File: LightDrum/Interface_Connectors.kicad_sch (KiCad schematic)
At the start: 6 parts, among them J6 0525593652, J7 0541323662, J8 PWR-CONN

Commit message: General component placement
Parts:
- J1203: renamed from J8; footprint Connector_JST:JST_XA_B02B-XASK-1_1x02_P2.50mm_Vertical -> Daxxn_Connectors:JST_XH_B2B-XH-A_Vertical
- renumbered C88 to C1201, C89 to C1202, C90 to C1203, J6 to J1201, J7 to J1202
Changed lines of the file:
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@@
   (symbol (lib_id "Device:C_Small") (at 31.75 22.86 0) (unit 1)
     (in_bom yes) (on_board yes)
-    (property "Reference" "C90" (id 0) (at 32.004 21.082 0)
+    (property "Reference" "C1203" (id 0) (at 32.004 21.082 0)
       (effects (font (size 1.27 1.27)) (justify left))
     )
@@
   (symbol (lib_id "power:GND") (at 50.8 93.98 0) (unit 1)
     (in_bom yes) (on_board yes)
-    (property "Reference" "#PWR0134" (id 0) (at 50.8 100.33 0)
+    (property "Reference" "#PWR01212" (id 0) (at 50.8 100.33 0)
       (effects (font (size 1.27 1.27)) hide)
     )
@@
   (symbol (lib_id "power:VCC") (at 25.4 20.32 0) (unit 1)
     (in_bom yes) (on_board yes)
-    (property "Reference" "#PWR0128" (id 0) (at 25.4 24.13 0)
+    (property "Reference" "#PWR01202" (id 0) (at 25.4 24.13 0)
       (effects (font (size 1.27 1.27)) hide)
     )
@@
   (symbol (lib_id "Daxxn_Connectors:0541323662") (at 123.19 86.36 0) (unit 1)
     (in_bom no) (on_board no)
-    (property "Reference" "J7" (id 0) (at 124.46 38.1 0))
+    (property "Reference" "J1202" (id 0) (at 124.46 38.1 0))
     (property "Value" "0541323662" (id 1) (at 124.46 40.64 0))
     (property "Footprint" "Daxxn_Connectors:0541323662" (id 2) (at 123.19 86.36 0)
@@
   (symbol (lib_id "power:VCC") (at 19.05 20.32 0) (unit 1)
     (in_bom yes) (on_board yes)
-    (property "Reference" "#PWR0127" (id 0) (at 19.05 24.13 0)
+    (property "Reference" "#PWR01201" (id 0) (at 19.05 24.13 0)
       (effects (font (size 1.27 1.27)) hide)
     )
@@
   (symbol (lib_id "power:GND") (at 25.4 25.4 0) (unit 1)
     (in_bom yes) (on_board yes)
-    (property "Reference" "#PWR0129" (id 0) (at 25.4 31.75 0)
+    (property "Reference" "#PWR01205" (id 0) (at 25.4 31.75 0)
       (effects (font (size 1.27 1.27)) hide)
     )
@@
   (symbol (lib_id "power:GND") (at 124.46 137.16 0) (unit 1)
     (in_bom yes) (on_board yes)
-    (property "Reference" "#PWR0133" (id 0) (at 124.46 143.51 0)
+    (property "Reference" "#PWR01216" (id 0) (at 124.46 143.51 0)
       (effects (font (size 1.27 1.27)) hide)
     )
@@
   (symbol (lib_id "Device:C_Small") (at 25.4 22.86 0) (unit 1)
     (in_bom yes) (on_board yes)
-    (property "Reference" "C89" (id 0) (at 25.654 21.082 0)
+    (property "Reference" "C1202" (id 0) (at 25.654 21.082 0)
       (effects (font (size 1.27 1.27)) (justify left))
     )
@@
   (symbol (lib_id "Device:C_Small") (at 19.05 22.86 0) (unit 1)
     (in_bom yes) (on_board yes)
-    (property "Reference" "C88" (id 0) (at 19.304 21.082 0)
+    (property "Reference" "C1201" (id 0) (at 19.304 21.082 0)
       (effects (font (size 1.27 1.27)) (justify left))
     )
@@
   (symbol (lib_id "power:VCC") (at 69.85 44.45 0) (unit 1)
     (in_bom yes) (on_board yes)
-    (property "Reference" "#PWR0123" (id 0) (at 69.85 48.26 0)
+    (property "Reference" "#PWR01210" (id 0) (at 69.85 48.26 0)
       (effects (font (size 1.27 1.27)) hide)
     )
@@
   (symbol (lib_id "power:GND") (at 50.8 114.3 0) (unit 1)
     (in_bom yes) (on_board yes)
-    (property "Reference" "#PWR0135" (id 0) (at 50.8 120.65 0)
+    (property "Reference" "#PWR01214" (id 0) (at 50.8 120.65 0)
       (effects (font (size 1.27 1.27)) hide)
     )
@@
   (symbol (lib_id "power:VCC") (at 91.44 40.64 0) (unit 1)
     (in_bom yes) (on_board yes)
-    (property "Reference" "#PWR0125" (id 0) (at 91.44 44.45 0)
+    (property "Reference" "#PWR01207" (id 0) (at 91.44 44.45 0)
       (effects (font (size 1.27 1.27)) hide)
     )
@@
   (symbol (lib_id "power:VCC") (at 31.75 20.32 0) (unit 1)
     (in_bom yes) (on_board yes)
-    (property "Reference" "#PWR0130" (id 0) (at 31.75 24.13 0)
+    (property "Reference" "#PWR01203" (id 0) (at 31.75 24.13 0)
       (effects (font (size 1.27 1.27)) hide)
     )
@@
   (symbol (lib_id "power:GND") (at 31.75 25.4 0) (unit 1)
     (in_bom yes) (on_board yes)
-    (property "Reference" "#PWR0131" (id 0) (at 31.75 31.75 0)
+    (property "Reference" "#PWR01206" (id 0) (at 31.75 31.75 0)
       (effects (font (size 1.27 1.27)) hide)
     )
@@
   (symbol (lib_id "power:Vdrive") (at 99.06 40.64 0) (unit 1)
     (in_bom yes) (on_board yes)
-    (property "Reference" "#PWR0132" (id 0) (at 93.98 44.45 0)
+    (property "Reference" "#PWR01208" (id 0) (at 93.98 44.45 0)
       (effects (font (size 1.27 1.27)) hide)
     )
@@
   (symbol (lib_id "power:VDD") (at 97.79 128.27 0) (unit 1)
     (in_bom yes) (on_board yes)
-    (property "Reference" "#PWR069" (id 0) (at 97.79 132.08 0)
+    (property "Reference" "#PWR01215" (id 0) (at 97.79 132.08 0)
       (effects (font (size 1.27 1.27)) hide)
     )
@@
   (symbol (lib_id "power:Vdrive") (at 63.5 44.45 0) (unit 1)
     (in_bom yes) (on_board yes)
-    (property "Reference" "#PWR0124" (id 0) (at 58.42 48.26 0)
+    (property "Reference" "#PWR01209" (id 0) (at 58.42 48.26 0)
       (effects (font (size 1.27 1.27)) hide)
     )
@@
   (symbol (lib_id "Connector:Conn_01x02_Male") (at 57.15 110.49 0) (mirror y) (unit 1)
     (in_bom yes) (on_board yes)
-    (property "Reference" "J8" (id 0) (at 58.42 110.49 0)
+    (property "Reference" "J1203" (id 0) (at 58.42 110.49 0)
       (effects (font (size 1.27 1.27)) (justify right))
     )
@@
       (effects (font (size 1.27 1.27)) (justify right))
     )
-    (property "Footprint" "Connector_JST:JST_XA_B02B-XASK-1_1x02_P2.50mm_Vertical" (id 2) (at 57.15 110.49 0)
+    (property "Footprint" "Daxxn_Connectors:JST_XH_B2B-XH-A_Vertical" (id 2) (at 57.15 110.49 0)
       (effects (font (size 1.27 1.27)) hide)
     )
@@
   (symbol (lib_id "power:VDD") (at 29.21 88.9 0) (unit 1)
     (in_bom yes) (on_board yes)
-    (property "Reference" "#PWR068" (id 0) (at 29.21 92.71 0)
+    (property "Reference" "#PWR01211" (id 0) (at 29.21 92.71 0)
       (effects (font (size 1.27 1.27)) hide)
     )
@@
   (symbol (lib_id "power:GND") (at 19.05 25.4 0) (unit 1)
     (in_bom yes) (on_board yes)
-    (property "Reference" "#PWR0126" (id 0) (at 19.05 31.75 0)
+    (property "Reference" "#PWR01204" (id 0) (at 19.05 31.75 0)
       (effects (font (size 1.27 1.27)) hide)
     )
@@
   (symbol (lib_id "power:VCC") (at 50.8 109.22 0) (unit 1)
     (in_bom yes) (on_board yes)
-    (property "Reference" "#PWR0136" (id 0) (at 50.8 113.03 0)
+    (property "Reference" "#PWR01213" (id 0) (at 50.8 113.03 0)
       (effects (font (size 1.27 1.27)) hide)
     )
@@
   (symbol (lib_id "Daxxn_Connectors:0525593652") (at 52.07 71.12 180) (unit 1)
     (in_bom yes) (on_board yes)
-    (property "Reference" "J6" (id 0) (at 50.8 40.64 0))
+    (property "Reference" "J1201" (id 0) (at 50.8 40.64 0))
     (property "Value" "0525593652" (id 1) (at 50.8 43.18 0))
     (property "Footprint" "Daxxn_Connectors:0525593652" (id 2) (at 50.8 99.06 0)

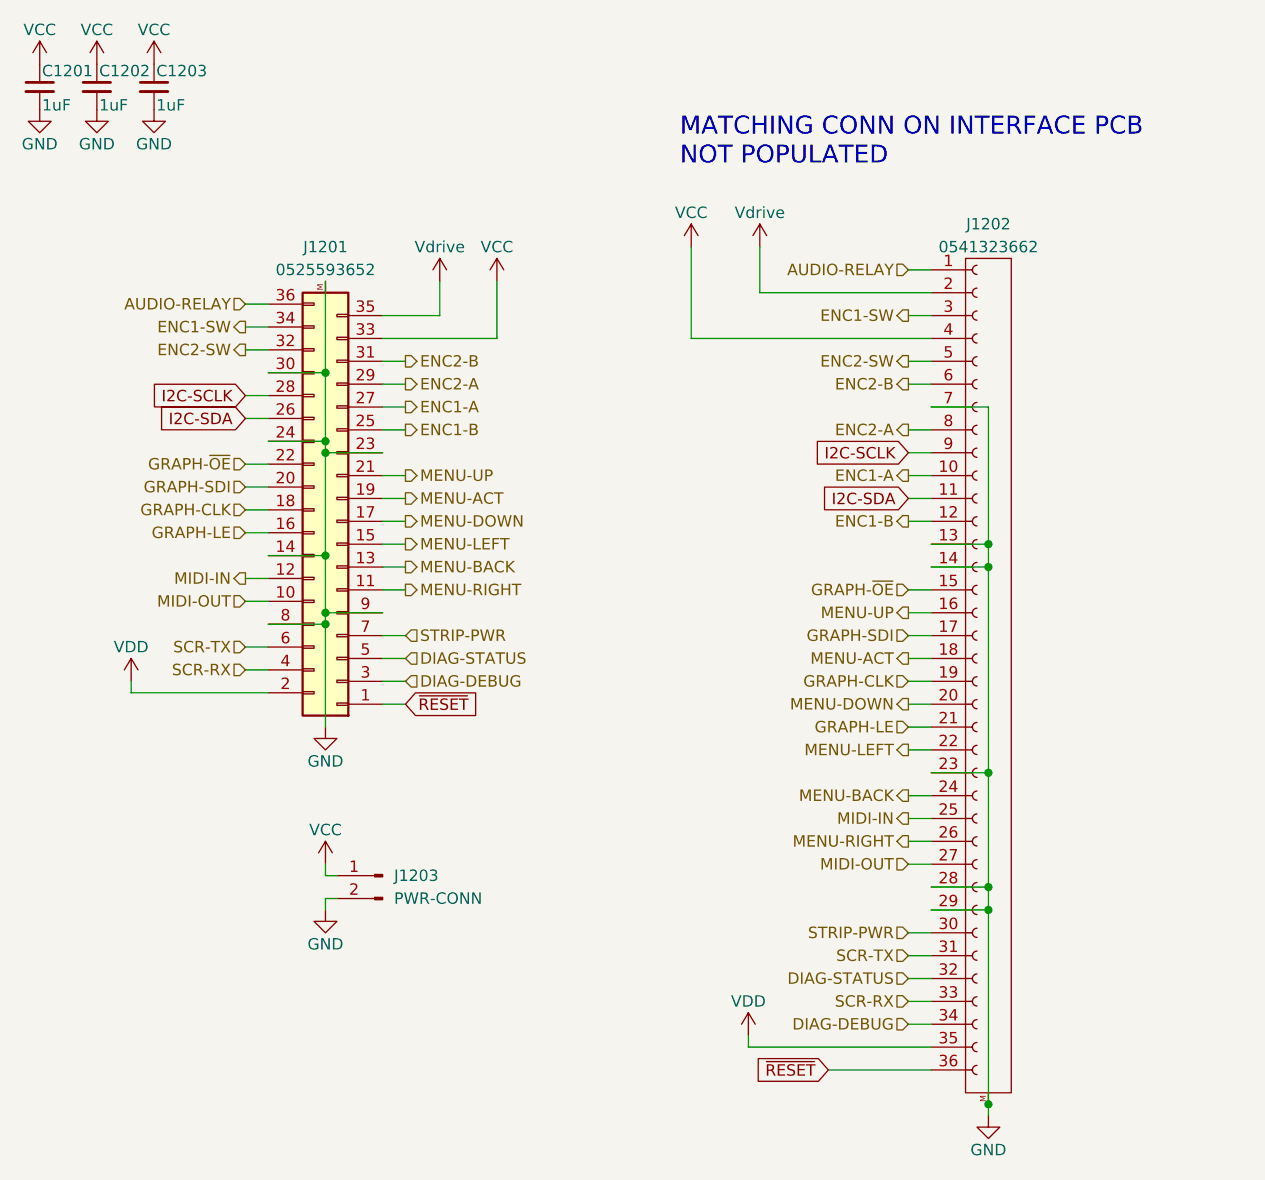
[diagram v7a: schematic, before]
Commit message: Replace with smaller case (WIP)
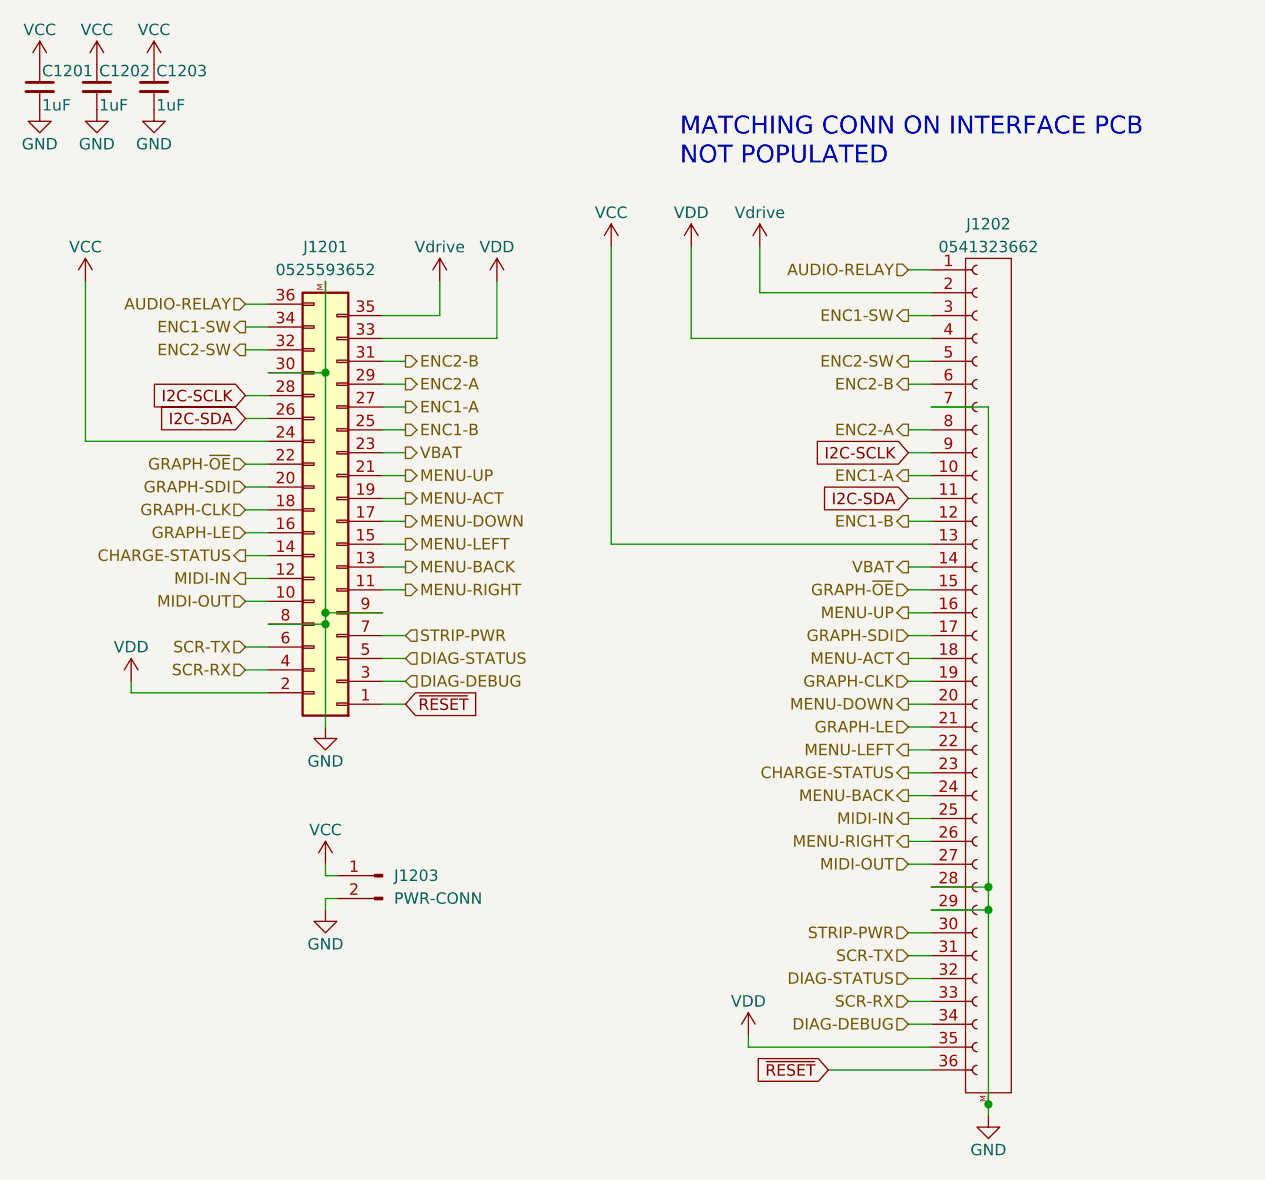
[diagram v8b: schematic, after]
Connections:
- net GND: no longer J1201.14 (Pin_14), J1201.23 (Pin_23), J1201.24 (Pin_24), J1202.13 (Pin_13), J1202.14 (Pin_14), J1202.23 (Pin_23)
- net VCC: now also J1201.24 (Pin_24), J1202.13 (Pin_13); no longer J1201.33 (Pin_33), J1202.4 (Pin_4)
- net VDD: now also J1201.33 (Pin_33), J1202.4 (Pin_4)
- new net CHARGE-STATUS: J1201.14 (Pin_14), J1202.23 (Pin_23)
- new net VBAT: J1201.23 (Pin_23), J1202.14 (Pin_14)
